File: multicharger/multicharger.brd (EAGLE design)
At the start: 26 x 57 mm, 25 parts, among them J2 USB-MICROA-AMPHENOL-10118192-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, J3 HEADER-8POS-, P1 TEST-POINT, P2 TEST-POINT, P3 TEST-POINT, P4 TEST-POINT, P5 TEST-POINT, P6 TEST-POINT, U1 MCP73831T-2ACI/OT, U2 MCP73831T-2ACI/OT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

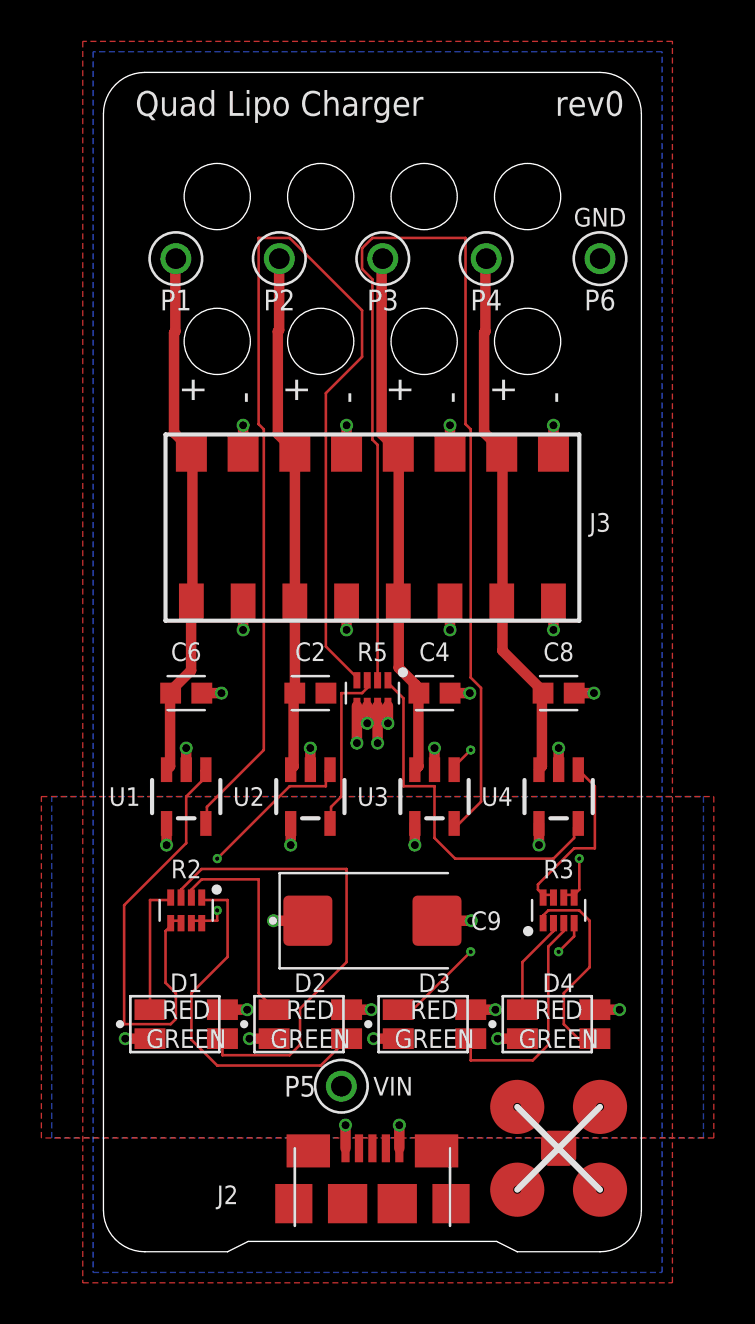
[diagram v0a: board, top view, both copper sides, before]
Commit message: smaller LEDs for multi-charger
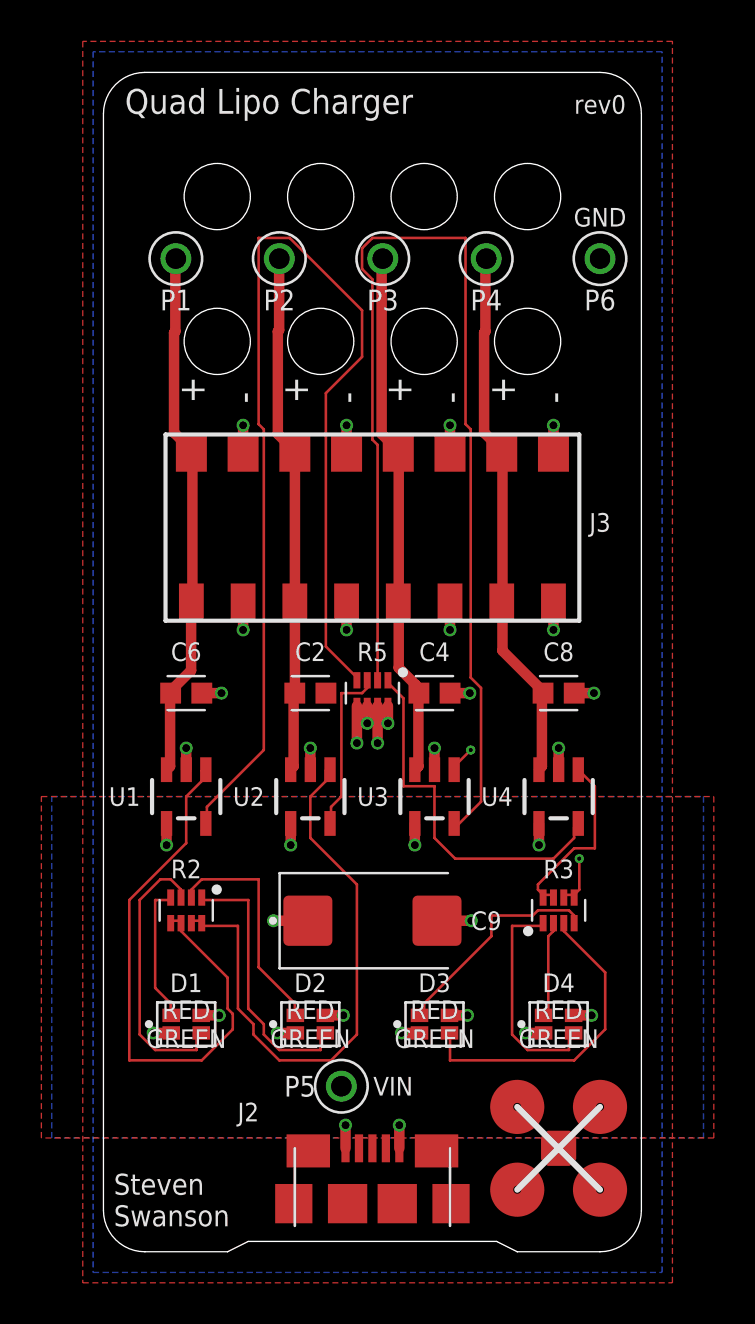
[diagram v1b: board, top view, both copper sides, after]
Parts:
- D1, D2, D3, D4: value LED-2X-GREEN/RED -> LED-2X-GREEN/RED-1.6X1.5MM; device RemoteParts:LED-2X-LTST-C155 -> RemoteParts:LED-2X-LITE-ON-1.6MMX1.5MM
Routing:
- net N$3: track 12.1 -> 28.4 mm, vias 2 -> 0
- net N$1: track 23.0 -> 13.5 mm
- net N$11: track 22.3 -> 28.2 mm
- net N$5: track 17.4 -> 13.2 mm
- net N$9: track 11.3 -> 15.4 mm
- net VIN: track 11.7 -> 10.4 mm
- net GND: track 30.6 -> 29.3 mm
- net N$6: track 10.4 -> 11.1 mm
- net N$15: track 10.3 -> 10.9 mm
- net N$10: track 10.6 -> 10.9 mm, vias 2 -> 0
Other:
- board text added: "Steven Swanson"

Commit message: make file, better-looking layout
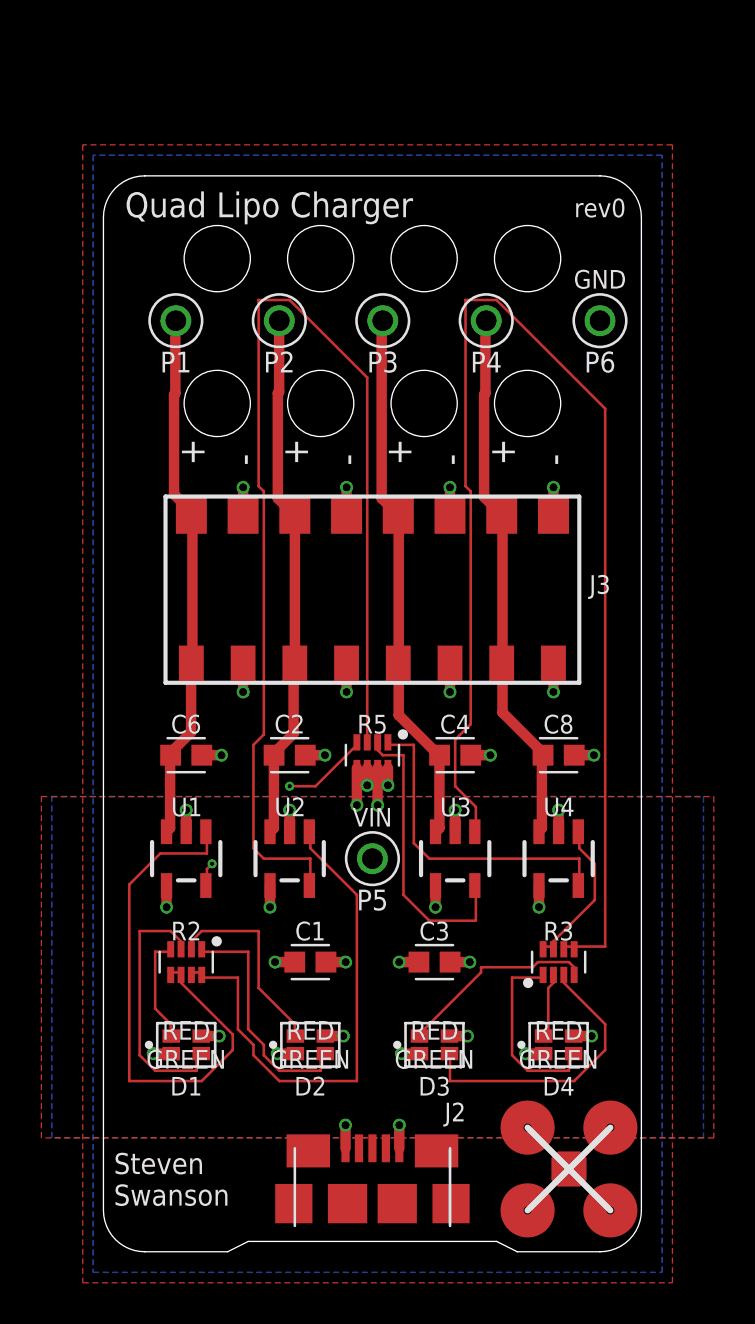
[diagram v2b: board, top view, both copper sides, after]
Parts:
- removed C9: 220uF, quadparts_prebuilt:CAPMP7343X310_HS
- added C1, C3: 10uF, quadparts_prebuilt:CAPC1608X100
- moved P5 11.1 mm to (0.00, -3.00)
- moved C2 3.16 mm to (-4.00, 2.00)
- moved C4 3.16 mm to (4.00, 2.00)
- moved U2 3.16 mm to (-4.00, -3.00)
- moved U3 3.16 mm to (4.00, -3.00)
- moved C6 3.00 mm to (-9.00, 2.00)
- moved C8 3.00 mm to (9.00, 2.00)
- moved J3 3.00 mm to (0.00, 10.0)
- moved P1 3.00 mm to (-9.50, 23.0)
- moved P2 3.00 mm to (-4.50, 23.0)
- moved P3 3.00 mm to (0.50, 23.0)
- moved P4 3.00 mm to (5.50, 23.0)
- moved P6 3.00 mm to (11.0, 23.0)
- moved R5 3.00 mm to (0.00, 2.00)
- moved U1 3.00 mm to (-9.00, -3.00)
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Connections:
- net GND: now also C1.2, C3.2; no longer C9.2
- net VIN: now also C1.1, C3.1; no longer C9.1
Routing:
- net N$7: track 11.3 -> 63.7 mm, vias 2 -> 0
- net N$4: track 8.25 -> 55.5 mm
- net N$12: track 55.2 -> 10.7 mm, vias 0 -> 2
- net N$8: track 55.9 -> 14.2 mm
- net N$3: track 28.4 -> 25.2 mm
- net N$11: track 28.2 -> 26.0 mm
- net N$14: track 17.8 -> 15.8 mm
- net N$9: track 15.4 -> 13.9 mm
- net N$6: track 11.1 -> 9.64 mm
- net N$5: track 13.2 -> 11.7 mm
- net N$2: track 6.76 -> 5.26 mm
- net N$16: track 4.72 -> 3.22 mm
- net N$15: track 10.9 -> 9.43 mm
- net N$13: track 8.97 -> 7.47 mm
- net N$10: track 10.9 -> 9.70 mm
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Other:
- board size 26 x 57 mm -> 26 x 52 mm

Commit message: routed
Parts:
- moved P1 0.50 mm to (-10.0, 23.0)
- moved P2 0.50 mm to (-5.00, 23.0)
- moved P3 0.50 mm to (0.00, 23.0)
- moved P4 0.50 mm to (5.00, 23.0)
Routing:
- net N$4: track 55.5 -> 57.4 mm
- net N$7: track 63.7 -> 65.0 mm
